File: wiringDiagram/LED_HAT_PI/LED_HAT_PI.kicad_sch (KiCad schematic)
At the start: 14 parts, among them J1 Raspberry_Pi_2_3, U1 KWM-20882CVB

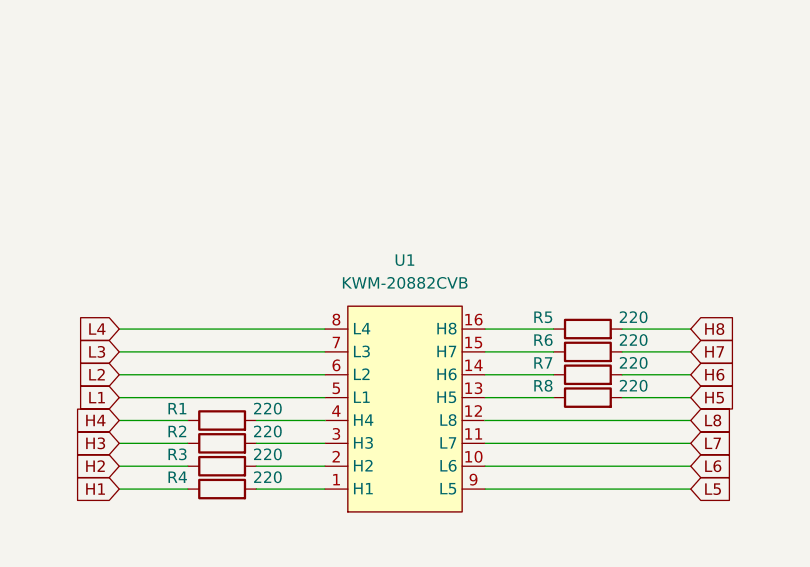
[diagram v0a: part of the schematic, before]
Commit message: Fixed library paths
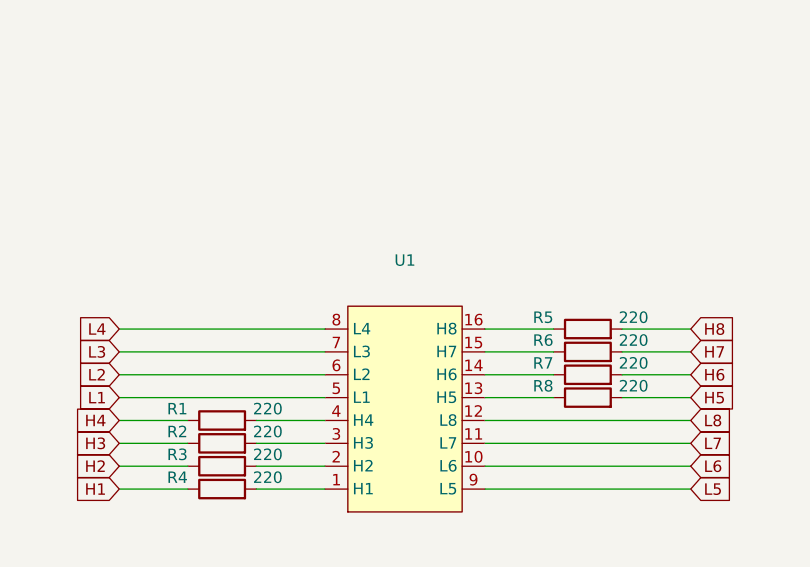
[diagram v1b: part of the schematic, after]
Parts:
- U1: value KWM-20882CVB -> (none); footprint pi_hat_footprint:DIPS4572W51P254L6020H925Q16N -> (none)
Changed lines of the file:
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@@
     (in_bom yes) (on_board yes) (fields_autoplaced)
     (property "Reference" "U1" (id 0) (at 195.58 80.01 90))
-    (property "Value" "KWM-20882CVB" (id 1) (at 195.58 82.55 90))
-    (property "Footprint" "pi_hat_footprint:DIPS4572W51P254L6020H925Q16N" (id 2) (at 179.07 96.52 0)
+    (property "Value" "" (id 1) (at 195.58 82.55 90))
+    (property "Footprint" "" (id 2) (at 179.07 96.52 0)
       (effects (font (size 1.27 1.27)) hide)
     )
